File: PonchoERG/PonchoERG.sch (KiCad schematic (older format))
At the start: 1 part

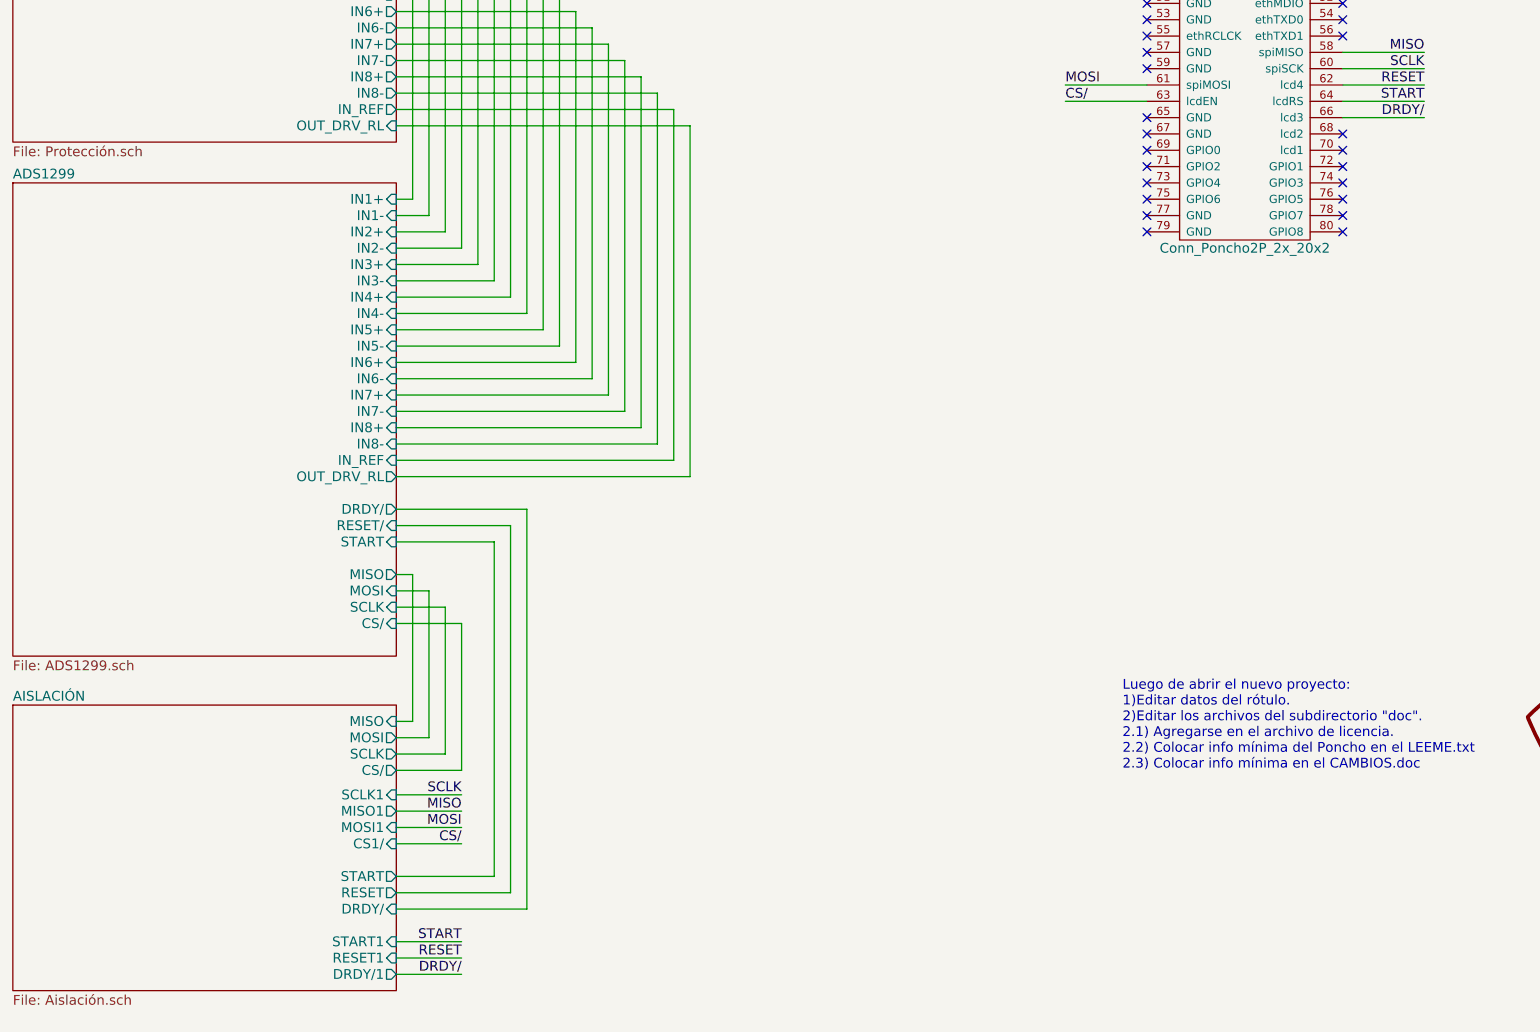
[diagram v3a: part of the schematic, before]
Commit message: Inclusión en esquemáticos de los nuevos bloques de circuitos para la utilización de las líneas del BIAS. Actualización de librería de proyecto. Objetivo de este comit: revisar actualización e inclusión de BIAS.
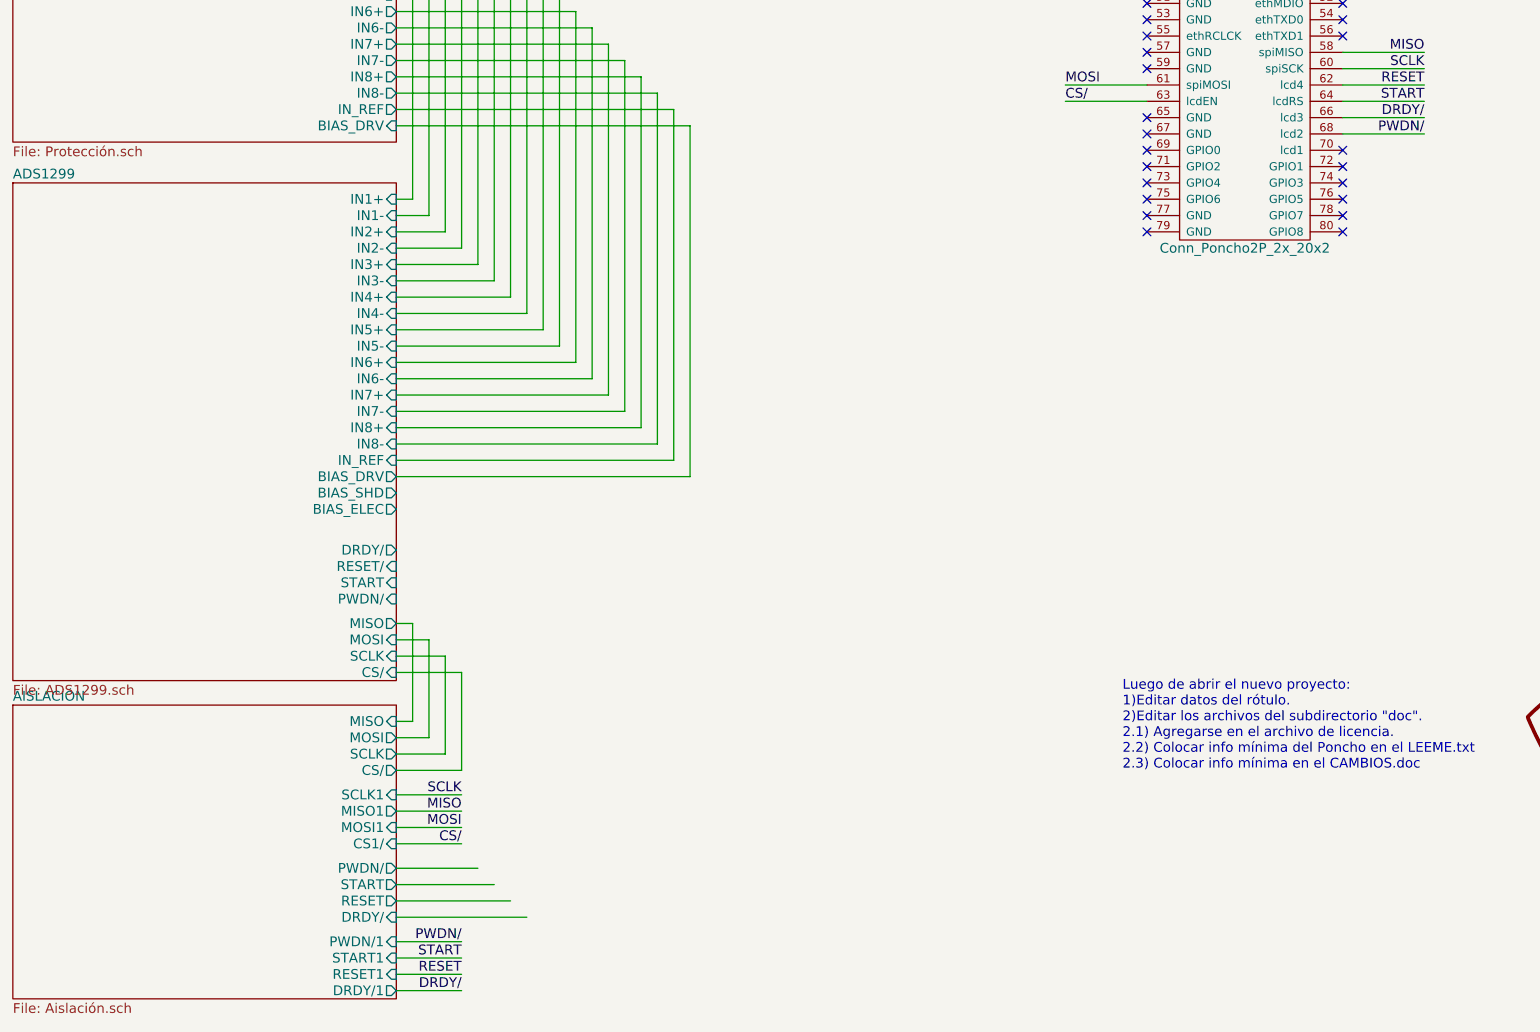
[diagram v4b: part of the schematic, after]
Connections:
- net labels added: PWDN/
- wire segments 91 -> 88
- no-connect marks 31 -> 30
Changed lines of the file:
@@
 LIBS:PonchoERG
 LIBS:power
+LIBS:74xgxx
+LIBS:74xx
+LIBS:ac-dc
+LIBS:actel
+LIBS:adc-dac
+LIBS:Altera
+LIBS:analog_devices
+LIBS:analog_switches
+LIBS:atmel
+LIBS:audio
+LIBS:brooktre
+LIBS:cmos_ieee
+LIBS:cmos4000
+LIBS:conn
+LIBS:contrib
+LIBS:cypress
+LIBS:dc-dc
+LIBS:device
+LIBS:digital-audio
+LIBS:diode
+LIBS:display
+LIBS:dsp
+LIBS:elec-unifil
+LIBS:ESD_Protection
+LIBS:ftdi
+LIBS:gennum
+LIBS:graphic
+LIBS:hc11
+LIBS:intel
+LIBS:interface
+LIBS:ir
+LIBS:Lattice
+LIBS:linear
+LIBS:logo
+LIBS:maxim
+LIBS:memory
+LIBS:microchip
+LIBS:microchip_dspic33dsc
+LIBS:microchip_pic10mcu
+LIBS:microchip_pic12mcu
+LIBS:microchip_pic16mcu
+LIBS:microchip_pic18mcu
+LIBS:microchip_pic32mcu
+LIBS:microcontrollers
+LIBS:motor_drivers
+LIBS:motorola
+LIBS:msp430
+LIBS:nordicsemi
+LIBS:nxp_armmcu
+LIBS:onsemi
+LIBS:opto
+LIBS:Oscillators
+LIBS:philips
+LIBS:Power_Management
+LIBS:powerint
+LIBS:pspice
+LIBS:references
+LIBS:regul
+LIBS:relays
+LIBS:rfcom
+LIBS:sensors
+LIBS:silabs
+LIBS:siliconi
+LIBS:stm8
+LIBS:stm32
+LIBS:supertex
+LIBS:switches
+LIBS:texas
+LIBS:transf
+LIBS:transistors
+LIBS:ttl_ieee
+LIBS:valves
+LIBS:video
+LIBS:Xicor
+LIBS:xilinx
+LIBS:Zilog
 LIBS:PonchoERG-cache
 EELAYER 25 0
@@
 F17 "IN8-" O R 2900 2150 60
 F18 "IN_REF" O R 2900 2250 60
-F19 "OUT_DRV_RL" I R 2900 2350 60
+F19 "BIAS_DRV" I R 2900 2350 60
 $EndSheet
 $Sheet
-S 550  2700 2350 2900
+S 550  2700 2350 3050
 U 57BDC369
 F0 "ADS1299" 60
@@
 F17 "IN8-" I R 2900 4300 60
 F18 "IN_REF" I R 2900 4400 60
-F19 "OUT_DRV_RL" O R 2900 4500 60
-F20 "DRDY/" O R 2900 4700 60
-F21 "MISO" O R 2900 5100 60
-F22 "MOSI" I R 2900 5200 60
-F23 "RESET/" I R 2900 4800 60
-F24 "START" I R 2900 4900 60
-F25 "SCLK" I R 2900 5300 60
-F26 "CS/" I R 2900 5400 60
+F19 "DRDY/" O R 2900 4950 60
+F20 "MISO" O R 2900 5400 60
+F21 "MOSI" I R 2900 5500 60
+F22 "RESET/" I R 2900 5050 60
+F23 "START" I R 2900 5150 60
+F24 "SCLK" I R 2900 5600 60
+F25 "CS/" I R 2900 5700 60
+F26 "PWDN/" I R 2900 5250 60
+F27 "BIAS_DRV" O R 2900 4500 60
+F28 "BIAS_SHD" O R 2900 4600 60
+F29 "BIAS_ELEC" O R 2900 4700 60
 $EndSheet
 $Sheet
-S 550  5900 2350 1750
+S 550  5900 2350 1800
 U 57BDC3A8
 F0 "AISLACIÓN" 60
@@
 F4 "SCLK" O R 2900 6200 60
 F5 "CS/" O R 2900 6300 60
-F6 "START1" I R 2900 7350 60
-F7 "RESET1" I R 2900 7450 60
-F8 "DRDY/1" O R 2900 7550 60
-F9 "RESET" O R 2900 7050 60
-F10 "START" O R 2900 6950 60
-F11 "DRDY/" I R 2900 7150 60
+F6 "START1" I R 2900 7450 60
+F7 "RESET1" I R 2900 7550 60
+F8 "DRDY/1" O R 2900 7650 60
+F9 "RESET" O R 2900 7100 60
+F10 "START" O R 2900 7000 60
+F11 "DRDY/" I R 2900 7200 60
 F12 "MISO1" O R 2900 6550 60
 F13 "MOSI1" I R 2900 6650 60
 F14 "SCLK1" I R 2900 6450 60
 F15 "CS1/" I R 2900 6750 60
+F16 "PWDN/1" I R 2900 7350 60
+F17 "PWDN/" O R 2900 6900 60
 $EndSheet
 Wire Wire Line
@@
 	4500 2150 2900 2150
 Wire Wire Line
-	2900 5100 3000 5100
-Wire Wire Line
-	3000 5100 3000 6000
-Wire Wire Line
 	3000 6000 2900 6000
 Wire Wire Line
 	2900 6100 3100 6100
 Wire Wire Line
-	3100 6100 3100 5200
-Wire Wire Line
-	3100 5200 2900 5200
-Wire Wire Line
-	2900 5300 3200 5300
-Wire Wire Line
-	3200 5300 3200 6200
-Wire Wire Line
 	3200 6200 2900 6200
 Wire Wire Line
 	2900 6300 3300 6300
-Wire Wire Line
-	3300 6300 3300 5400
-Wire Wire Line
-	3300 5400 2900 5400
-Wire Wire Line
-	2900 4900 3500 4900
-Wire Wire Line
-	3500 4900 3500 6950
-Wire Wire Line
-	3500 6950 2900 6950
-Wire Wire Line
-	2900 7050 3600 7050
-Wire Wire Line
-	3600 7050 3600 4800
-Wire Wire Line
-	3600 4800 2900 4800
-Wire Wire Line
-	2900 4700 3700 4700
-Wire Wire Line
-	3700 4700 3700 7150
-Wire Wire Line
-	3700 7150 2900 7150
 Wire Wire Line
 	2900 2350 4700 2350
@@
 	2900 6750 3300 6750
 Wire Wire Line
-	2900 7350 3300 7350
-Wire Wire Line
 	2900 7450 3300 7450
 Wire Wire Line
 	2900 7550 3300 7550
+Wire Wire Line
+	2900 7650 3300 7650
 Text Label 3300 6450 2    60   ~ 0
 SCLK
@@
 Text Label 3300 6750 2    60   ~ 0
 CS/
-Text Label 3300 7350 2    60   ~ 0
+Text Label 3300 7450 2    60   ~ 0
 START
-Text Label 3300 7450 2    60   ~ 0
+Text Label 3300 7550 2    60   ~ 0
 RESET
-Text Label 3300 7550 2    60   ~ 0
+Text Label 3300 7650 2    60   ~ 0
 DRDY/
 NoConn ~ 7500 1100
@@
 NoConn ~ 8700 2600
 NoConn ~ 8700 2500
-NoConn ~ 8700 2400
 NoConn ~ 8700 1800
 NoConn ~ 8700 1700
@@
 NoConn ~ 8700 1300
 NoConn ~ 8700 1200
+Wire Wire Line
+	3400 6900 2900 6900
+Wire Wire Line
+	2900 7000 3500 7000
+Wire Wire Line
+	3600 7100 2900 7100
+Wire Wire Line
+	2900 7200 3700 7200
+Wire Wire Line
+	2900 7350 3300 7350
+Text Label 3300 7350 2    60   ~ 0
+PWDN/
+Wire Wire Line
+	8700 2400 9200 2400
+Text Label 9200 2400 2    60   ~ 0
+PWDN/
+Wire Wire Line
+	3000 6000 3000 5400
+Wire Wire Line
+	3000 5400 2900 5400
+Wire Wire Line
+	2900 5500 3100 5500
+Wire Wire Line
+	3100 5500 3100 6100
+Wire Wire Line
+	3200 6200 3200 5600
+Wire Wire Line
+	3200 5600 2900 5600
+Wire Wire Line
+	2900 5700 3300 5700
+Wire Wire Line
+	3300 5700 3300 6300
 $EndSCHEMATC
